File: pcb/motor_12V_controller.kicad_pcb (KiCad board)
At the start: 2 copper layers, 68 x 48 mm, 39 parts, among them IC1 RP2040-ZERO, J1 01x02, J2 01x02, U1 AP63200WU, U2 L293D

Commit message: Fixed the PCB according to new 3.3V connections.
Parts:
- moved C1 15.5 mm to (132.3, 82.7)
- moved C2 15.5 mm to (129.3, 75.7)
- moved C3 15.5 mm to (134.5, 80.7)
- moved C5 15.5 mm to (145.3, 82.7)
- moved C6 15.5 mm to (147.6, 82.6)
- moved D1 15.5 mm to (142.3, 85.8)
- moved D6 15.5 mm to (160.0, 110.0)
- moved H2 15.5 mm to (180.3, 72.9)
- moved H4 15.5 mm to (180.3, 112.9)
- moved IC1 15.5 mm to (157.5, 91.4)
- moved J1 15.5 mm to (119.9, 80.4)
- moved L1 15.5 mm to (129.1, 82.4)
- moved R1 15.5 mm to (141.6, 92.4)
- moved R10 15.5 mm to (160.0, 108.5)
- moved R11 15.5 mm to (159.1, 108.5)
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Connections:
- IC1 pad 21: unconnected-(IC1-3V3-Pad21) -> +3.3V
- R1 pad 1: +5V -> +3.3V
- R2 pad 2: +5V -> +3.3V
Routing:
- net +5V: track 91.5 -> 57.1 mm
- net +3.3V: track 0.00 -> 24.6 mm
- net Bpin: track 4.45 -> 15.2 mm
- net Apin: track 4.51 -> 13.2 mm

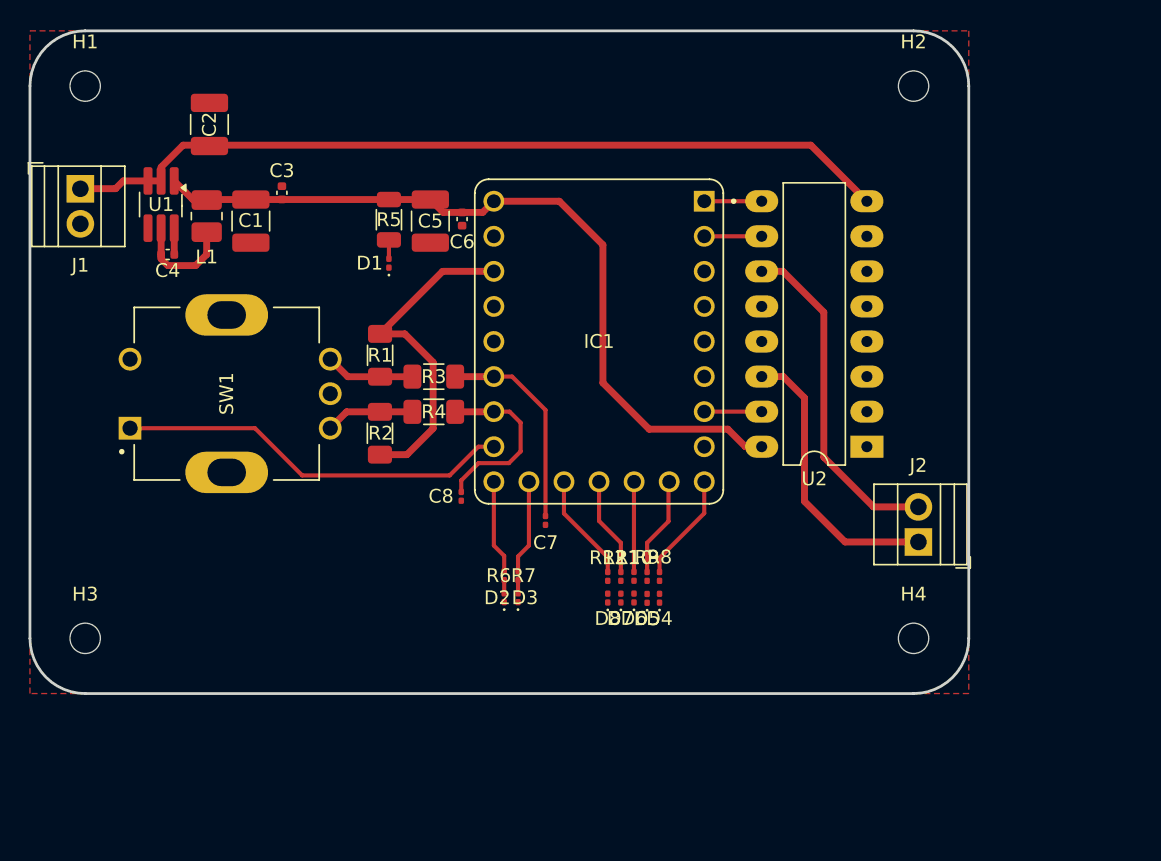
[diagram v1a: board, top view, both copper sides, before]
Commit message: Swapped the SMD schematic to the THT one. Adjusted the AP632xx circuit according to the layout specified in the datasheet.
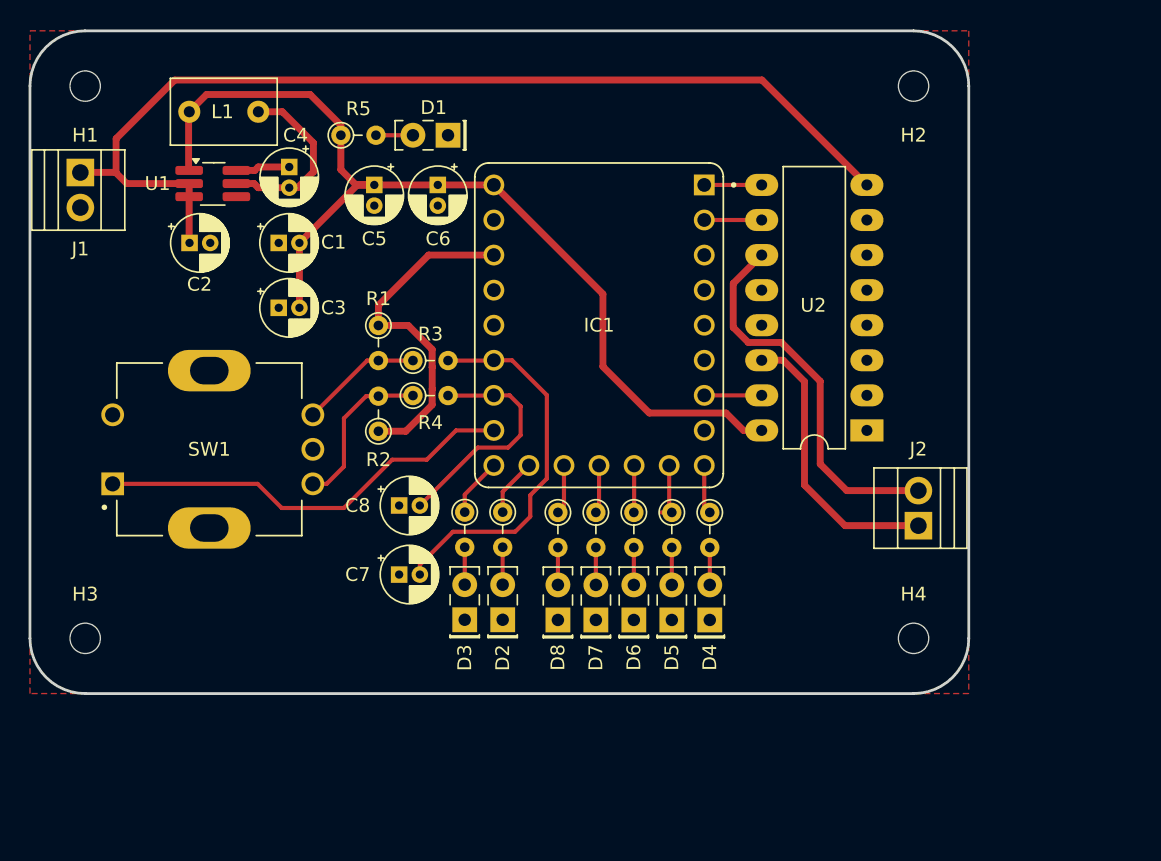
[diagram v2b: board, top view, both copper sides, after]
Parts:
- C1, C2, C5: footprint Capacitor_SMD:C_1210_3225Metric_Pad1.33x2.70mm_HandSolder -> Capacitor_THT:CP_Radial_D4.0mm_P1.50mm
- C3, C4, C6: footprint Capacitor_SMD:C_0402_1005Metric -> Capacitor_THT:CP_Radial_D4.0mm_P1.50mm
- C7, C8: footprint Capacitor_SMD:C_0201_0603Metric -> Capacitor_THT:CP_Radial_D4.0mm_P1.50mm
- D1, D2, D3, D4, D5, D6, D7, D8: footprint LED_SMD:LED_0201_0603Metric -> LED_THT:LED_Rectangular_W5.0mm_H2.0mm
- L1: footprint Inductor_SMD:L_1008_2520Metric_Pad1.43x2.20mm_HandSolder -> Inductor_THT:L_Radial_L7.5mm_W4.6mm_P5.00mm_Neosid_SD75
- R1, R2, R3, R4: footprint Resistor_SMD:R_1206_3216Metric_Pad1.30x1.75mm_HandSolder -> Resistor_THT:R_Axial_DIN0204_L3.6mm_D1.6mm_P2.54mm_Vertical
- R10, R11, R12, R6, R7, R8, R9: footprint Resistor_SMD:R_0201_0603Metric -> Resistor_THT:R_Axial_DIN0204_L3.6mm_D1.6mm_P2.54mm_Vertical
- R5: footprint Resistor_SMD:R_1206_3216Metric -> Resistor_THT:R_Axial_DIN0204_L3.6mm_D1.6mm_P2.54mm_Vertical
- moved C7 11.3 mm to (143.0, 108.3), turned to 0 degrees
- moved C4 10.9 mm to (135.0, 78.8), turned to -90 degrees
- moved D1 10.2 mm to (146.5, 76.5), turned to 180 degrees
- moved C2 8.70 mm to (127.8, 84.3), turned to 0 degrees
- moved L1 8.43 mm to (132.8, 74.8), turned to 180 degrees
- moved C3 8.33 mm to (134.3, 89.0), turned to 0 degrees
- moved R5 7.04 mm to (138.8, 76.5), turned to 0 degrees
- moved R8 5.89 mm to (165.5, 103.8)
- moved R12 5.87 mm to (154.5, 103.8)
- moved R7 5.42 mm to (147.8, 103.8)
- moved R11 4.98 mm to (157.2, 103.8)
- moved R9 4.97 mm to (162.8, 103.8)
- moved C5 4.83 mm to (141.2, 80.1)
- moved R6 4.73 mm to (150.5, 103.8)
- moved R10 4.63 mm to (160.0, 103.8)
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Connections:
- C1 pad 1: +5V -> GND
- C1 pad 2: GND -> +5V
- C3 pad 1: +5V -> GND
- C3 pad 2: GND -> +5V
- C6 pad 1: GND -> +5V
- C6 pad 2: +5V -> GND
- C7 pad 1: Bpin -> GND
- C7 pad 2: GND -> Bpin
- C8 pad 1: Apin -> GND
- C8 pad 2: GND -> Apin
- R2 pad 1: Net-(R2-Pad1) -> +3.3V
- R2 pad 2: +3.3V -> Net-(R2-Pad2)
- R4 pad 1: Net-(R2-Pad1) -> Net-(R2-Pad2)
- SW1 pad A: Net-(R2-Pad1) -> Net-(R2-Pad2)
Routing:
- net +5V: track 57.1 -> 73.4 mm
- net +12V: track 60.5 -> 74.3 mm
- net Bpin: track 15.2 -> 27.7 mm
- net Net-(R2-Pad2): track 0.00 -> 12.3 mm
- net Net-(R2-Pad1): track 6.44 -> 0.00 mm
- net Net-(U1-SW): track 7.68 -> 13.2 mm
- net S1: track 7.88 -> 3.57 mm
- net S5: track 7.85 -> 3.58 mm
- net S4: track 7.19 -> 3.50 mm
- net Apin: track 13.2 -> 16.7 mm
- net S2: track 7.20 -> 3.75 mm
- net Net-(J2-Pin_2): track 24.6 -> 27.9 mm
- net S3: track 6.53 -> 3.44 mm
- net Net-(D8-A): track 0.00 -> 2.71 mm
- net Net-(D7-A): track 0.00 -> 2.71 mm
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
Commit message: Fixed the H-Bridge decoupling. Added additional capasitor for +12V power input.
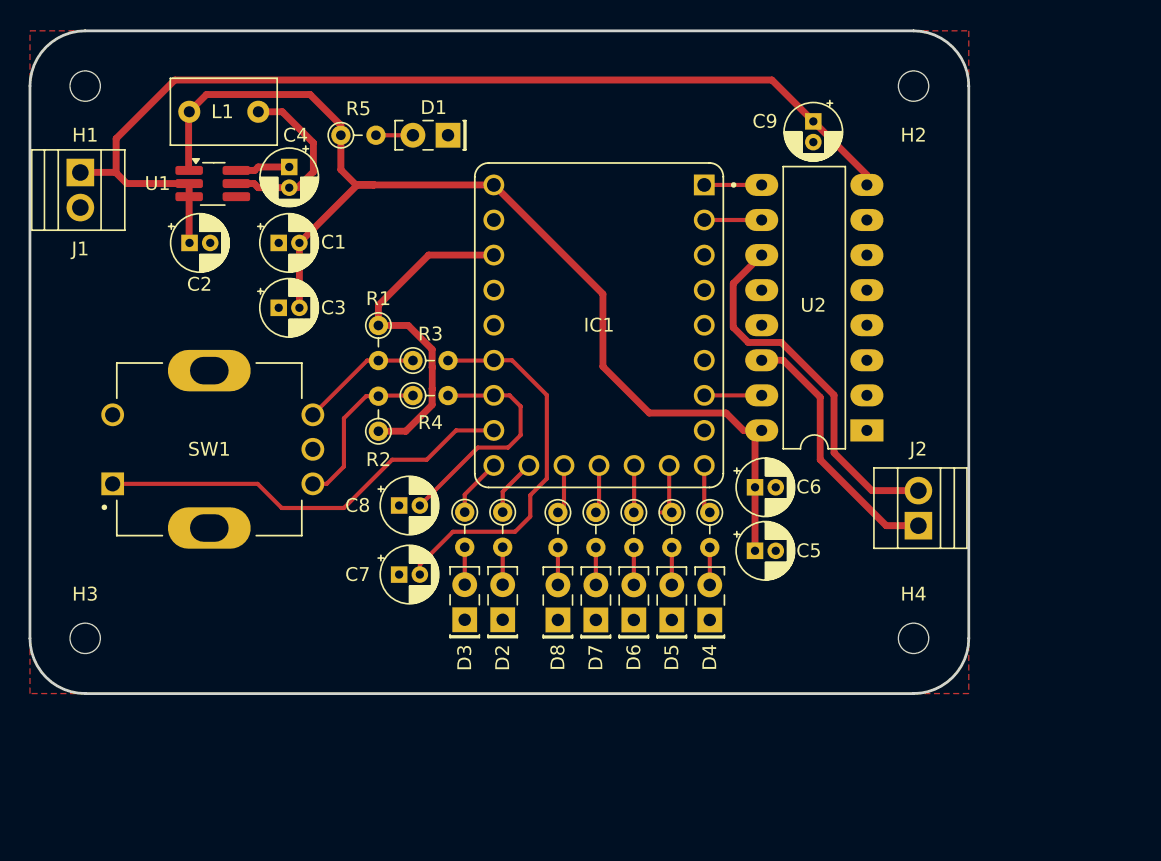
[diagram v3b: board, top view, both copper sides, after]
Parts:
- added C9: 100uf/25V, Capacitor_THT:CP_Radial_D4.0mm_P1.50mm, F.Cu at (173.0, 75.5)
- C1, C2: value 22uf -> 22uf/16V
- C5: value 10uf -> 100uf/6V
- moved C5 38.2 mm to (168.8, 106.6), turned to 0 degrees
- moved C6 31.7 mm to (168.8, 102.0), turned to 0 degrees
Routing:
- net +5V: track 73.4 -> 82.4 mm
- net Net-(J2-Pin_1): track 20.7 -> 19.0 mm
- net Net-(J2-Pin_2): track 27.9 -> 26.8 mm
